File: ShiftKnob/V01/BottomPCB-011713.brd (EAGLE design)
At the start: 32.6 x 32.6 mm, 20 parts, among them Q1 16MHz, U1 ATMEGA328, U2 MIC5205-5.0BM5

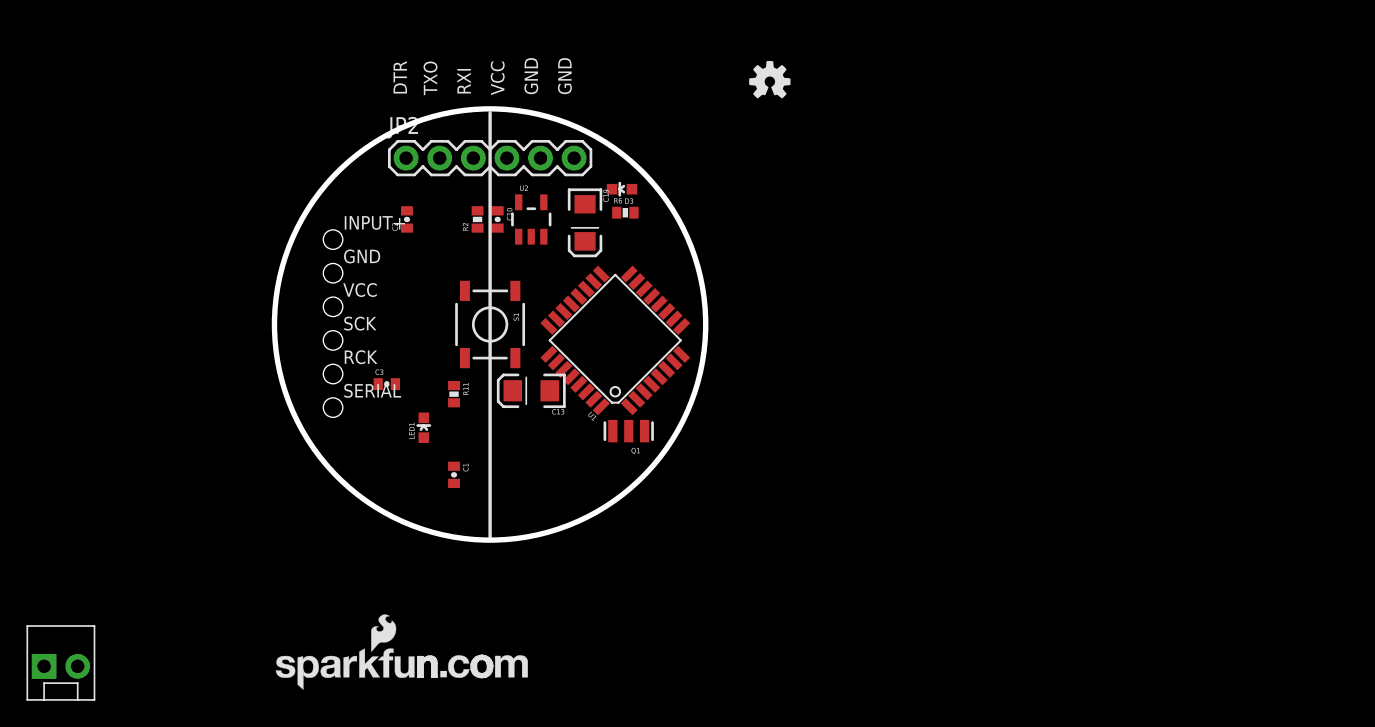
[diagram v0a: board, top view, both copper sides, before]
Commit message: all components added to BottomPCB schematic. added: MOSFETs, RGB LEDs x2, Motor connector, 7805 regulator
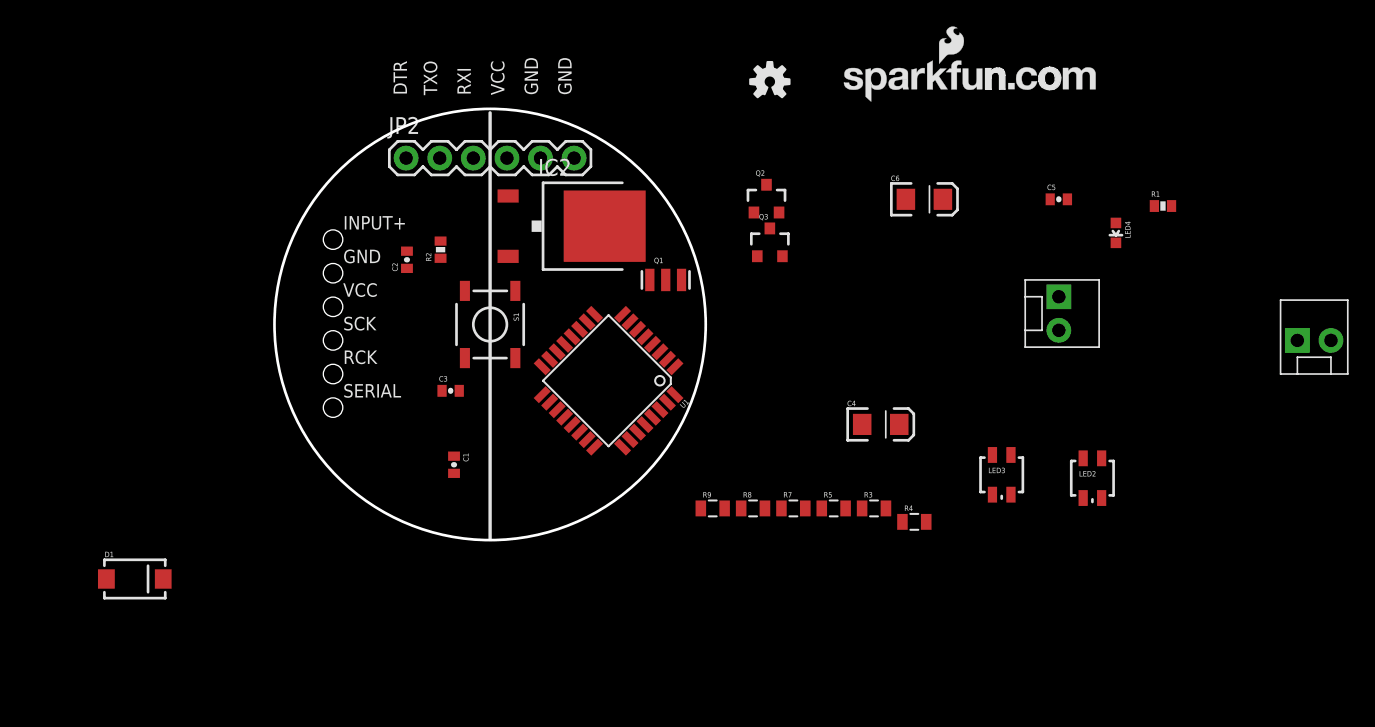
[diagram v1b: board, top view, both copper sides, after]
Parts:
- removed C10: 0.1uF, SparkFun:0402-CAP
- removed C13, C19: 10uF, SparkFun:EIA3216
- removed D3: Green, SparkFun:LED-0603
- removed LED1: Red, SparkFun:LED-0603
- removed R11: 10K, SparkFun:0402-RES
- removed R6: 330, SparkFun:0402-RES
- removed U2: MIC5205-5.0BM5, SparkFun:SOT23-5
- added C4, C6: 10uF, SparkFun:EIA3216
- added C5: 0.1uF, SparkFun:0402-CAP
- added D1: MBRA140, SparkFun-DiscreteSemi:SMA-DIODE
- added IC2: 7805DT, linear:TO252
- added JP4: PWM Motor Connection, SparkFun-Connectors:MOLEX-1X2
- added LED2, LED3: LED-TRICOLOR, SparkFun:LED-TRICOLOR-SMD
- added LED4: Red, SparkFun:LED-0603
- added Q2, Q3: MOSFET-NCHANNELSMD, SparkFun-DiscreteSemi:SOT23-3
- added R1: 10K, SparkFun:0402-RES
- added R3, R7: 50, SparkFun-Resistors:0805
- added R4, R5, R8, R9: 100, SparkFun-Resistors:0805
- JP3: value (none) -> 12V Battery Connection
- moved JP3 81.6 mm to (63.0, 22.1), turned to 270 degrees
- moved U$11 61.8 mm to (46.7, 36.8)
- moved JP1 12.7 mm to (8.13, 26.4), turned to 270 degrees
- moved Q1 11.8 mm to (33.3, 23.4), turned to 0 degrees
- moved C3 4.85 mm to (17.0, 15.0)
- moved R2 3.61 mm to (16.3, 25.7)
- moved U1 3.09 mm to (29.0, 15.7), turned to 225 degrees
- moved C2 3.05 mm to (13.7, 24.9)
- moved C1 0.76 mm to (17.3, 9.40)
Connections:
- removed net D4: U1.2
- removed net D5: U1.9
- removed net D6: U1.10
- removed net D7: U1.11
- removed net D8: U1.12
- removed net MISO: U1.16
- removed net MOSI: U1.15
- removed net N$38: LED1.A, R11.1
- removed net N$7: D3.A, R6.2
- removed net RCK: JP1.5
- removed net SCK: JP1.4, R6.1, U1.17
- removed net SERIAL: JP1.6
- new net 3.3V: Q2.3, Q3.3
- new net D11: R5.1, R9.1, U1.15
- new net D12: S1.3, S1.4, U1.16
- new net D13: U1.17
- new net D4/SERIAL: JP1.6, U1.2
- new net D5/MOTOR: Q2.1, U1.9
- new net D6/INPUT+: Q3.1, U1.10
- new net D7/RCK: JP1.5, U1.11
- new net D8/SCK: JP1.4, U1.12
- new net MOTOR+: D1.C, JP4.1, Q2.2
- new net N$16: LED3.B, R8.2
- new net N$25: LED2.B, R4.2
- new net N$3: LED4.A, R1.1
- new net N$4: LED2.R, R3.2
- new net N$5: LED2.G, R5.2
- new net N$6: LED3.R, R7.2
- new net N$8: LED3.G, R9.2
- net D10: now also R4.1, R8.1
- net D9: now also R3.1, R7.1
- net GND: now also C4.C, C5.2, C6.C, D1.A, IC2.3, JP4.2, LED2.A, LED3.A, LED4.C; no longer C10.2, C13.C, C19.C, D3.C, LED1.C, U2.2
- net INPUT+: now also Q3.2
- net RAW: now also C4.A, IC2.1; no longer C19.A, U2.1, U2.3
- net VCC: now also C5.1, C6.A, IC2.2, R1.2; no longer C10.1, C13.A, R11.2, U2.5

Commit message: all components on the board with no traces
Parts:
- added LED1: LED-TRICOLOR, SparkFun:LED-TRICOLOR-SMD
- added Q4, Q5, Q6: MOSFET-NCHANNELSMD, SparkFun-DiscreteSemi:SOT23-3
- added R10, R11: 100, SparkFun-Resistors:0805
- added R6: 50, SparkFun-Resistors:0805
- JP3, JP4: device SparkFun-Connectors:MOLEX-1X2 -> SparkFun-Connectors:JST-2-SMD
- moved JP4 61.3 mm to (20.6, 8.89), flipped to the bottom, turned to 90 degrees
- moved LED3 54.3 mm to (5.59, 20.1)
- moved LED2 45.4 mm to (27.2, 32.8), turned to 240 degrees
- moved R1 43.6 mm to (27.4, 25.7)
- moved LED4 40.0 mm to (27.4, 24.4), turned to 270 degrees
- moved R7 38.9 mm to (5.33, 16.0), turned to 90 degrees
- moved R8 37.6 mm to (6.86, 24.1), turned to 270 degrees
- moved R9 36.3 mm to (5.33, 24.1), turned to 270 degrees
- moved C5 35.6 mm to (27.4, 27.2), turned to 180 degrees
- moved JP3 35.6 mm to (27.4, 19.8), flipped to the bottom, turned to 180 degrees
- moved Q2 35.0 mm to (14.0, 7.11), turned to 90 degrees
- moved C6 32.9 mm to (23.6, 14.2), turned to 90 degrees
- moved R4 32.9 mm to (19.8, 11.4)
- moved Q3 31.2 mm to (10.2, 30.0), turned to 225 degrees
- moved R3 30.5 mm to (19.8, 15.0)
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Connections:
- removed net 3.3V: Q2.3, Q3.3
- new net N$10: LED1.G, R11.2
- new net N$11: Q4.1, U1.13
- new net N$12: Q5.1, U1.14
- new net N$15: Q6.1, U1.15
- new net N$7: LED1.B, R10.2
- new net N$9: LED1.R, R6.2
- net D10: now also Q5.3, R10.1; no longer U1.14
- net D11: now also Q6.3, R11.1; no longer U1.15
- net D9: now also Q4.3, R6.1; no longer U1.13
- net GND: now also JP3.1, JP4.1, Q4.2, Q5.2, Q6.2; no longer JP3.2, JP4.2, LED2.A, LED3.A
- net MOTOR+: now also JP4.2; no longer JP4.1
- net RAW: now also JP3.2; no longer JP3.1
- net VCC: now also LED1.A, LED2.A, LED3.A, Q2.3, Q3.3

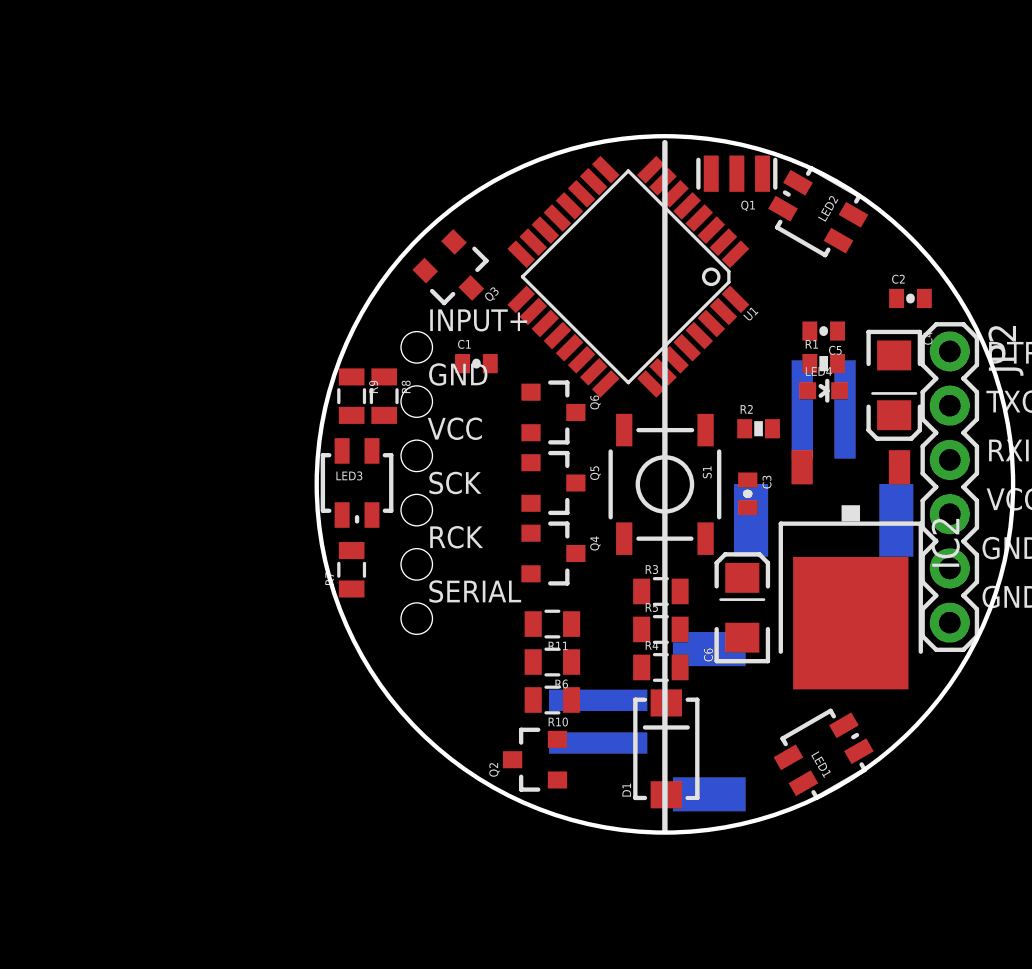
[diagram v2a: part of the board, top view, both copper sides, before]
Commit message: add pullup resistor to button. adding traces to board.
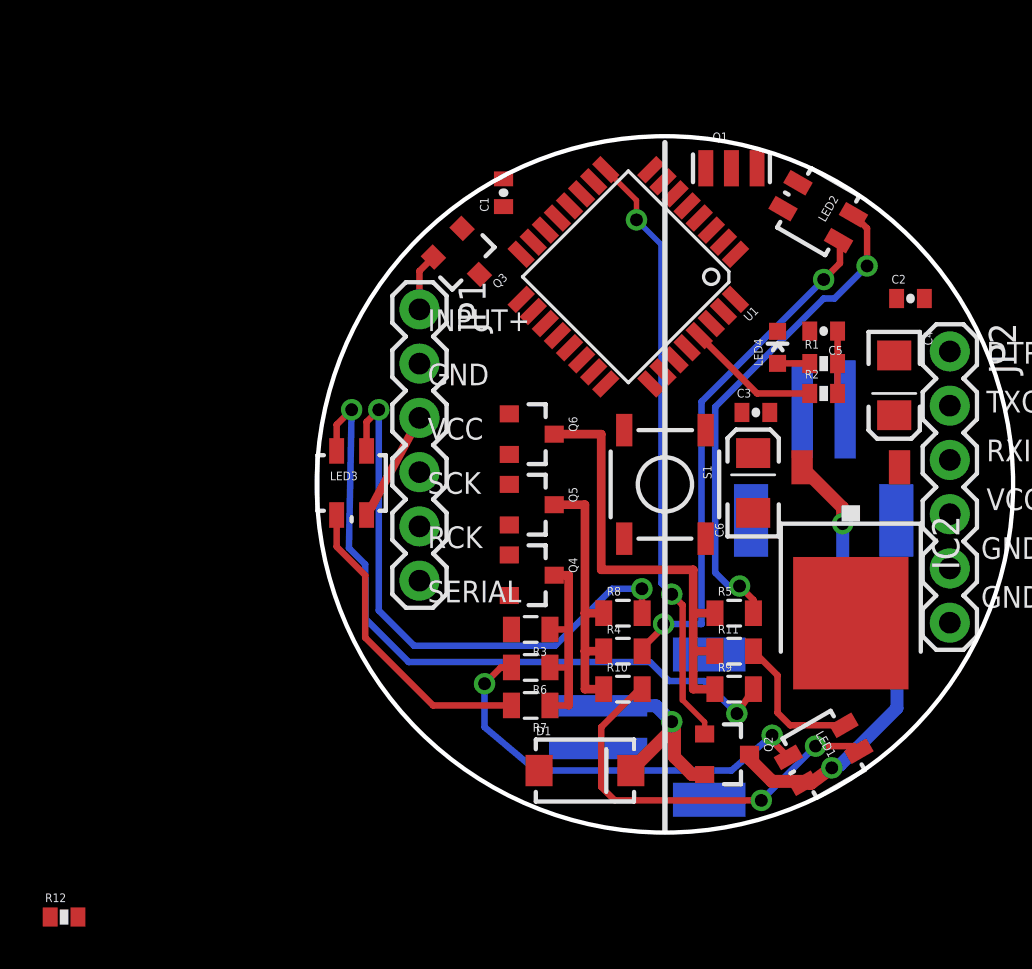
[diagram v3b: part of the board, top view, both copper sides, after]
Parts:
- added R12: 10k, SparkFun-Passives:0402-RES
- JP1: device SparkFun-Connectors:1X06_HOLES_ONLY -> SparkFun-Connectors:1X06
- moved R9 22.6 mm to (23.2, 10.4), turned to 0 degrees
- moved R8 15.1 mm to (18.0, 14.0), turned to 0 degrees
- moved R7 10.5 mm to (13.7, 9.65), turned to 180 degrees
- moved Q2 8.89 mm to (22.9, 7.37), turned to 270 degrees
- moved R11 8.60 mm to (23.2, 12.2), turned to 0 degrees
- moved C1 8.10 mm to (12.4, 33.7), turned to 90 degrees
- moved R3 6.35 mm to (13.7, 13.2), turned to 180 degrees
- moved C6 5.86 mm to (24.1, 20.1)
- moved D1 3.94 mm to (16.3, 6.60), turned to 0 degrees
- moved C3 3.83 mm to (24.3, 23.4), turned to 0 degrees
- moved R5 3.51 mm to (23.2, 14.0)
- moved R2 3.47 mm to (27.4, 24.3)
- moved R10 3.34 mm to (18.0, 10.4), turned to 0 degrees
- moved LED4 2.96 mm to (25.3, 26.4), turned to 0 degrees
- moved R4 1.93 mm to (18.0, 12.2)
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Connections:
- new net 3.3V: R12.2
- net D12: now also R12.1
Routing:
- net N$8: track 0.00 -> 32.9 mm, vias 0 -> 2
- net VCC: track 0.00 -> 30.2 mm, vias 0 -> 2
- net D5/MOTOR: track 0.00 -> 28.3 mm, vias 0 -> 2
- net N$16: track 0.00 -> 26.8 mm, vias 0 -> 2
- net N$25: track 0.00 -> 24.1 mm, vias 0 -> 2
- net N$5: track 0.00 -> 23.2 mm, vias 0 -> 2
- net D11: track 0.00 -> 21.5 mm
- net N$9: track 0.00 -> 19.8 mm, vias 0 -> 2
- net N$7: track 0.00 -> 18.9 mm, vias 0 -> 2
- net N$6: track 0.00 -> 14.5 mm
- net D10: track 0.00 -> 12.7 mm
- net MOTOR+: track 0.00 -> 10.3 mm, vias 0 -> 1
- net D9: track 0.00 -> 9.41 mm
- net N$10: track 0.00 -> 6.70 mm
- net RESET: track 0.00 -> 6.30 mm
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
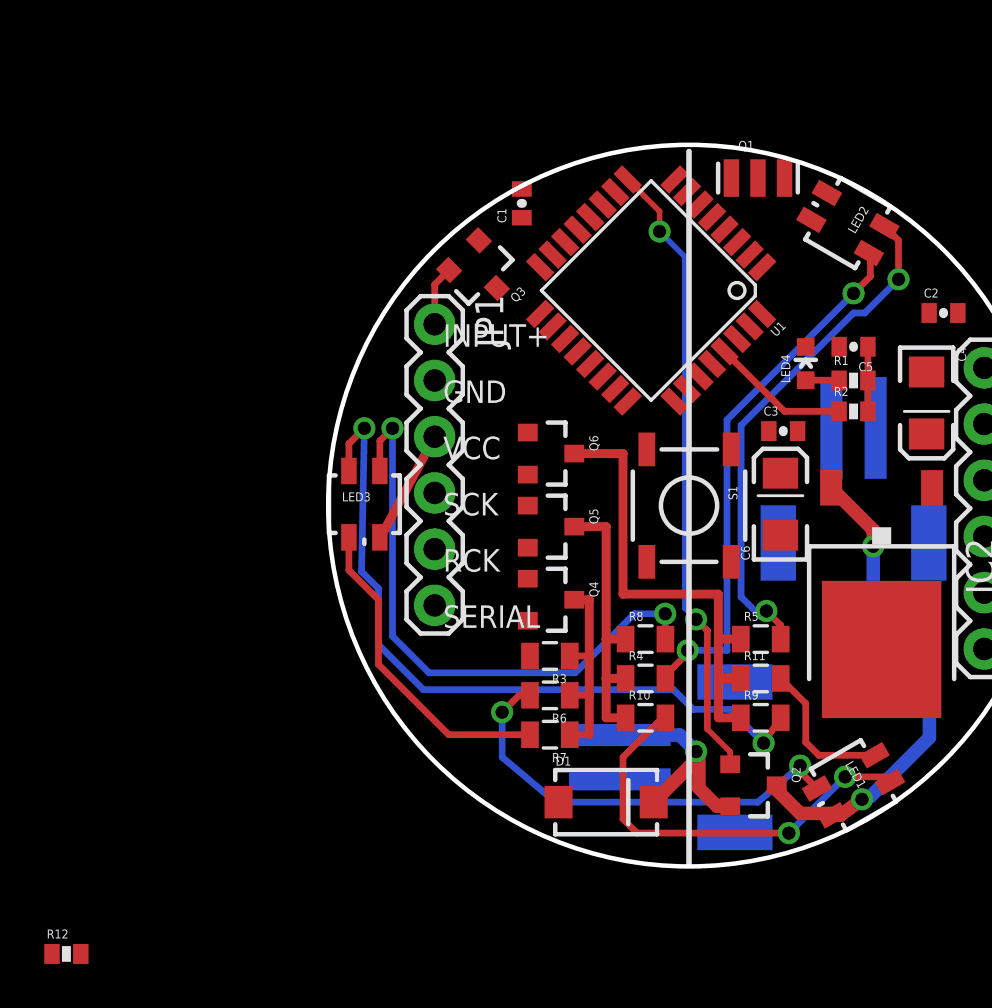
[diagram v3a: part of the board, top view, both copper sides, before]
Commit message: add more traces to brd layout. not yet finished.
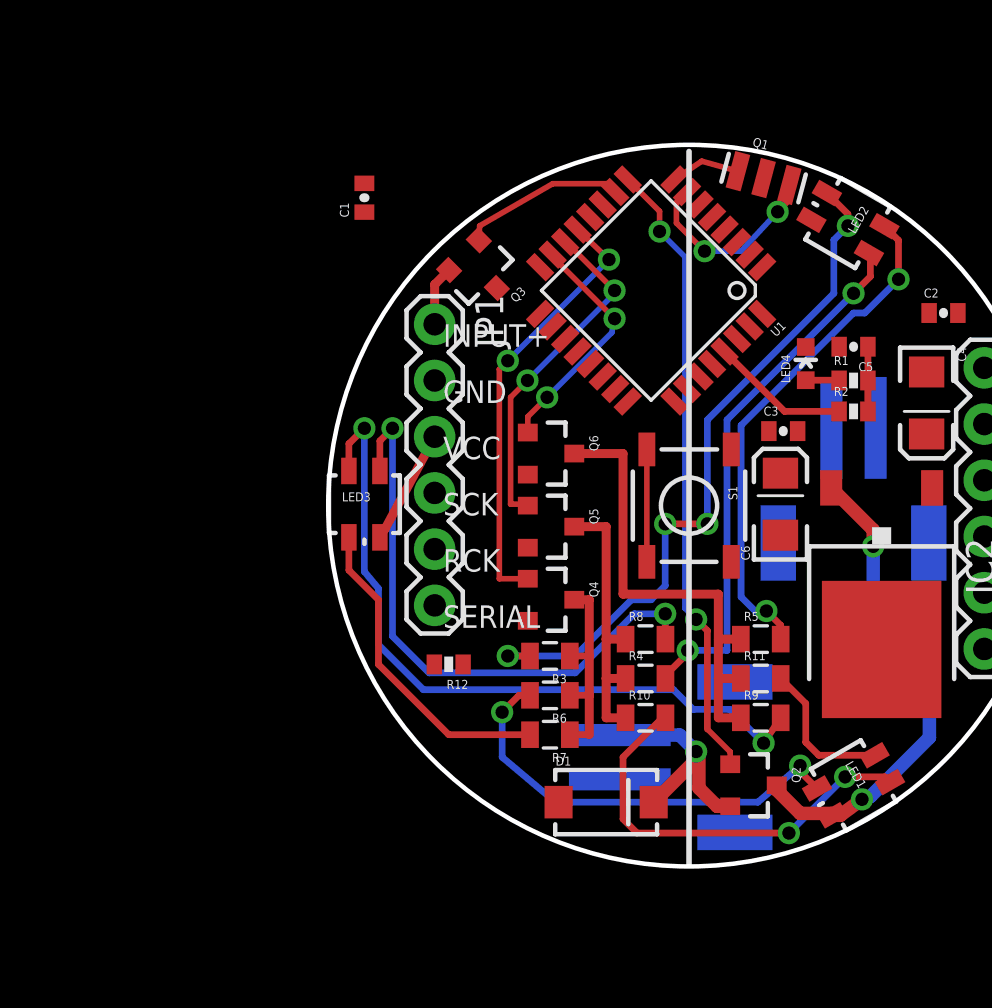
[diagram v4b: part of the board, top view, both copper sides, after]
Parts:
- moved R12 21.7 mm to (9.14, 12.8), turned to 180 degrees
- moved C1 7.12 mm to (5.33, 33.9)
- moved Q1 0.25 mm to (23.4, 34.8), turned to 345 degrees
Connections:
- removed net 3.3V: R12.2
- net VCC: now also R12.2
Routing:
- net N$4: track 0.00 -> 32.1 mm, vias 0 -> 4
- net N$11: track 0.00 -> 19.7 mm, vias 0 -> 2
- net N$12: track 0.00 -> 15.5 mm, vias 0 -> 2
- net N$15: track 0.00 -> 10.8 mm, vias 0 -> 2
- net N$2: track 0.00 -> 8.90 mm, vias 0 -> 2
- net D6/INPUT+: track 0.00 -> 7.45 mm
- net D12: track 0.00 -> 5.08 mm
- net N$1: track 0.00 -> 3.18 mm
